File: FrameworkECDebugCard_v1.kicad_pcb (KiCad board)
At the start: 2 copper layers, 26 x 30 mm, 25 parts, among them J1 Conn_01x05, P1 USB_C_Plug_USB2.0, P2 USB_B_Micro, U1 FT230XS

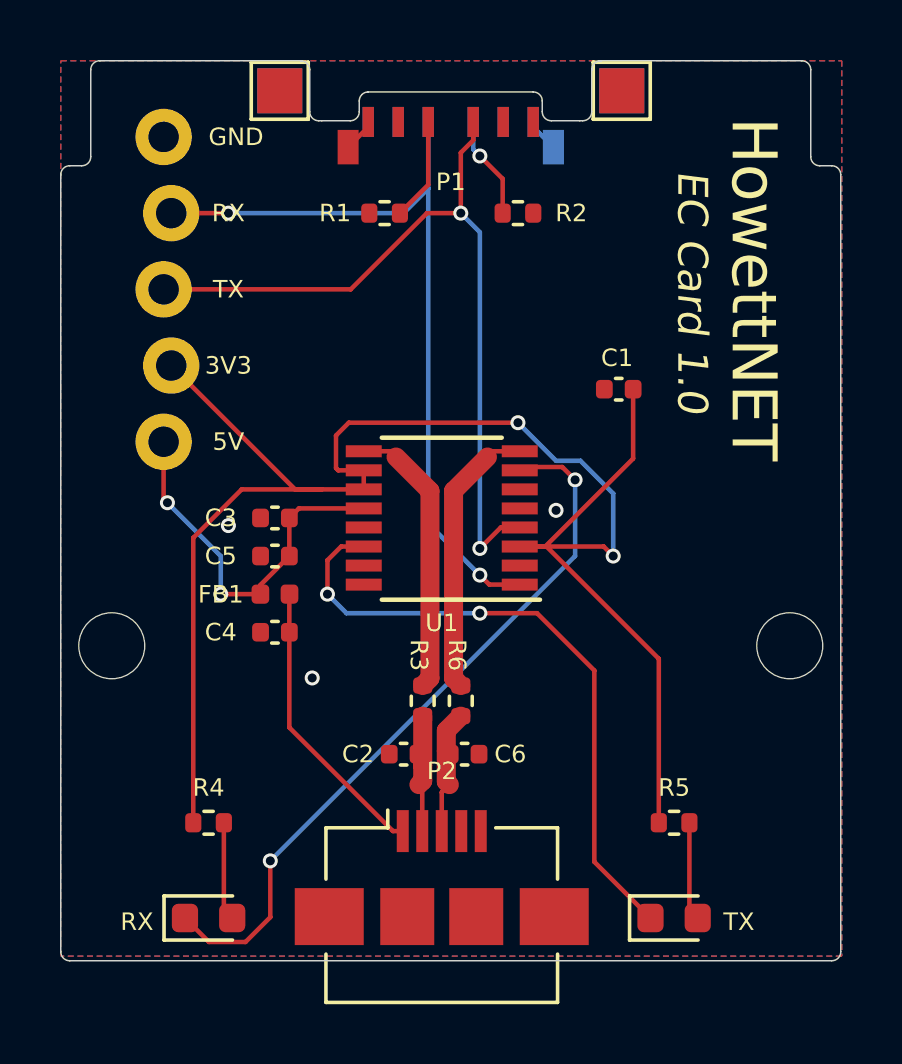
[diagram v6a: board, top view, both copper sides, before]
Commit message: Move the passives closer to USB, use 6mil traces to passives
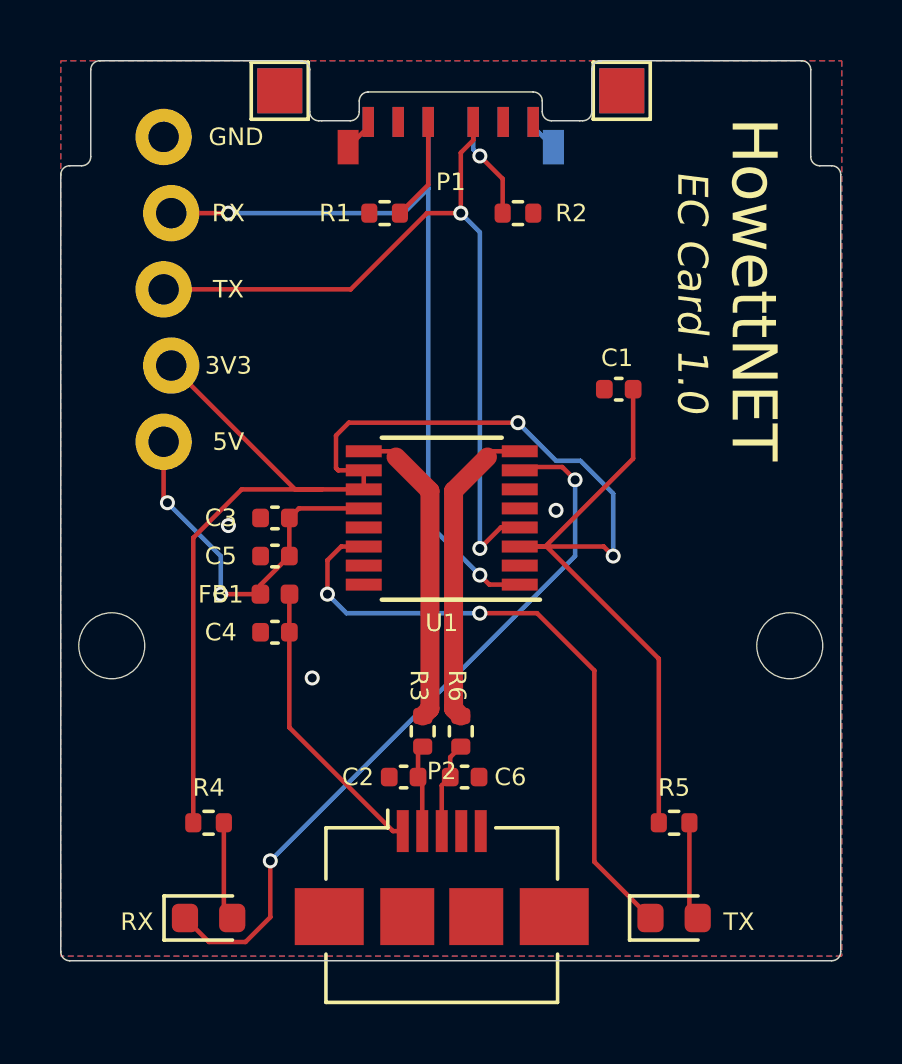
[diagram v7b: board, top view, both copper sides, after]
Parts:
- moved R3 1.02 mm to (139.1, 149.4)
- moved R6 1.02 mm to (140.3, 149.4)
- moved C2 0.76 mm to (138.4, 150.9)
- moved C6 0.76 mm to (140.5, 150.9)
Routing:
- net /USBD-: track 4.15 -> 2.94 mm
- net /USBD+: track 4.18 -> 3.08 mm
- net /F_USBD-: track 9.34 -> 10.4 mm
- net /F_USBD+: track 9.34 -> 10.4 mm
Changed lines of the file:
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@@
   )
   (footprint "Resistor_SMD:R_0402_1005Metric" (layer "F.Cu")
-    (at 139.065 148.336 90)
+    (at 139.065 149.352 90)
     (descr "Resistor SMD 0402 (1005 Metric), square (rectangular) end terminal, IPC_7351 nominal, (Body size source: IPC-SM-782 page 72, https://www.pcb-3d.com/wordpress/wp-content/uploads/ipc-sm-782a_amendment_1_and_2.pdf), generated with kicad-footprint-generator")
     (tags "resistor")
@@
   )
   (footprint "Resistor_SMD:R_0402_1005Metric" (layer "F.Cu")
-    (at 140.335 148.336 90)
+    (at 140.335 149.352 90)
     (descr "Resistor SMD 0402 (1005 Metric), square (rectangular) end terminal, IPC_7351 nominal, (Body size source: IPC-SM-782 page 72, https://www.pcb-3d.com/wordpress/wp-content/uploads/ipc-sm-782a_amendment_1_and_2.pdf), generated with kicad-footprint-generator")
     (tags "resistor")
@@
   )
   (footprint "Capacitor_SMD:C_0402_1005Metric" (layer "F.Cu")
-    (at 138.43 150.114 180)
+    (at 138.43 150.876 180)
     (descr "Capacitor SMD 0402 (1005 Metric), square (rectangular) end terminal, IPC_7351 nominal, (Body size source: IPC-SM-782 page 76, https://www.pcb-3d.com/wordpress/wp-content/uploads/ipc-sm-782a_amendment_1_and_2.pdf), generated with kicad-footprint-generator")
     (tags "capacitor")
@@
   )
   (footprint "Capacitor_SMD:C_0402_1005Metric" (layer "F.Cu")
-    (at 140.462 150.114)
+    (at 140.462 150.876)
     (descr "Capacitor SMD 0402 (1005 Metric), square (rectangular) end terminal, IPC_7351 nominal, (Body size source: IPC-SM-782 page 76, https://www.pcb-3d.com/wordpress/wp-content/uploads/ipc-sm-782a_amendment_1_and_2.pdf), generated with kicad-footprint-generator")
     (tags "capacitor")
@@
   (segment (start 132.334 143.51) (end 132.334 144.78) (width 0.1524) (layer "B.Cu") (net 8))
   (segment (start 130.556 141.732) (end 132.334 143.51) (width 0.1524) (layer "B.Cu") (net 8))
-  (segment (start 139.852001 149.328999) (end 139.852001 150.012001) (width 0.635) (layer "F.Cu") (net 9))
-  (segment (start 139.7 151.384) (end 139.954 151.13) (width 0.1524) (layer "F.Cu") (net 9))
-  (segment (start 140.335 148.846) (end 139.852001 149.328999) (width 0.635) (layer "F.Cu") (net 9))
-  (segment (start 139.852001 151.028001) (end 139.954 151.13) (width 0.635) (layer "F.Cu") (net 9))
-  (segment (start 139.7 152.6786) (end 139.7 151.384) (width 0.1524) (layer "F.Cu") (net 9))
-  (segment (start 139.852001 150.012001) (end 139.852001 151.028001) (width 0.635) (layer "F.Cu") (net 9))
-  (segment (start 139.05 152.6786) (end 139.05 151.242) (width 0.1524) (layer "F.Cu") (net 10))
-  (segment (start 139.065 151.003) (end 138.938 151.13) (width 0.635) (layer "F.Cu") (net 10))
-  (segment (start 138.91 150.34) (end 139.065 150.495) (width 0.1524) (layer "F.Cu") (net 10))
-  (segment (start 139.065 148.846) (end 139.065 150.495) (width 0.635) (layer "F.Cu") (net 10))
-  (segment (start 139.065 150.495) (end 139.065 151.003) (width 0.635) (layer "F.Cu") (net 10))
-  (segment (start 139.05 151.242) (end 138.938 151.13) (width 0.1524) (layer "F.Cu") (net 10))
+  (segment (start 139.982 150.215) (end 140.335 149.862) (width 0.1524) (layer "F.Cu") (net 9))
+  (segment (start 139.7 151.158) (end 139.7 152.6786) (width 0.1524) (layer "F.Cu") (net 9))
+  (segment (start 139.982 150.876) (end 139.982 150.215) (width 0.1524) (layer "F.Cu") (net 9))
+  (segment (start 139.982 150.876) (end 139.7 151.158) (width 0.1524) (layer "F.Cu") (net 9))
+  (segment (start 138.91 150.876) (end 138.91 150.017) (width 0.1524) (layer "F.Cu") (net 10))
+  (segment (start 138.91 150.876) (end 139.05 151.016) (width 0.1524) (layer "F.Cu") (net 10))
+  (segment (start 139.05 151.016) (end 139.05 152.6786) (width 0.1524) (layer "F.Cu") (net 10))
+  (segment (start 138.91 150.017) (end 139.065 149.862) (width 0.1524) (layer "F.Cu") (net 10))
   (segment (start 135.89 144.78) (end 135.89 143.6501) (width 0.1524) (layer "F.Cu") (net 11))
   (segment (start 135.89 143.6501) (end 136.3476 143.1925) (width 0.1524) (layer "F.Cu") (net 11))
@@
   (segment (start 144.145 143.51) (end 144.145 140.97) (width 0.1524) (layer "B.Cu") (net 12))
   (segment (start 133.985 153.67) (end 144.145 143.51) (width 0.1524) (layer "B.Cu") (net 12))
+  (segment (start 142.3 140.0175) (end 141.4145 140.0175) (width 0.1524) (layer "F.Cu") (net 13))
+  (segment (start 141.4145 140.0175) (end 141.224 140.208) (width 0.1524) (layer "F.Cu") (net 13))
   (segment (start 140.093501 141.338499) (end 141.224 140.208) (width 0.635) (layer "F.Cu") (net 13))
-  (segment (start 141.4145 140.0175) (end 141.224 140.208) (width 0.1524) (layer "F.Cu") (net 13))
-  (segment (start 140.093501 147.584501) (end 140.093501 141.338499) (width 0.635) (layer "F.Cu") (net 13))
-  (segment (start 140.335 147.826) (end 140.093501 147.584501) (width 0.635) (layer "F.Cu") (net 13))
-  (segment (start 142.3 140.0175) (end 141.4145 140.0175) (width 0.1524) (layer "F.Cu") (net 13))
+  (segment (start 140.335 148.842) (end 140.093501 148.600501) (width 0.635) (layer "F.Cu") (net 13))
+  (segment (start 140.093501 148.600501) (end 140.093501 141.338499) (width 0.635) (layer "F.Cu") (net 13))
+  (segment (start 139.306499 141.338499) (end 138.176 140.208) (width 0.635) (layer "F.Cu") (net 14))
+  (segment (start 139.306499 148.600501) (end 139.306499 141.338499) (width 0.635) (layer "F.Cu") (net 14))
+  (segment (start 139.065 148.842) (end 139.306499 148.600501) (width 0.635) (layer "F.Cu") (net 14))
+  (segment (start 137.9855 140.0175) (end 138.176 140.208) (width 0.1524) (layer "F.Cu") (net 14))
   (segment (start 137.1 140.0175) (end 137.9855 140.0175) (width 0.1524) (layer "F.Cu") (net 14))
-  (segment (start 139.065 147.826) (end 139.306499 147.584501) (width 0.635) (layer "F.Cu") (net 14))
-  (segment (start 139.306499 141.338499) (end 138.176 140.208) (width 0.635) (layer "F.Cu") (net 14))
-  (segment (start 137.9855 140.0175) (end 138.176 140.208) (width 0.1524) (layer "F.Cu") (net 14))
-  (segment (start 139.306499 147.584501) (end 139.306499 141.338499) (width 0.635) (layer "F.Cu") (net 14))
   (segment (start 143.1925 143.1925) (end 142.3 143.1925) (width 0.1524) (layer "F.Cu") (net 15))
   (segment (start 142.3 143.1925) (end 145.0975 143.1925) (width 0.1524) (layer "F.Cu") (net 15))

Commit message: Re-route VCCIO to move cap closer to 3V3OUT, reroute RXLED in the new space
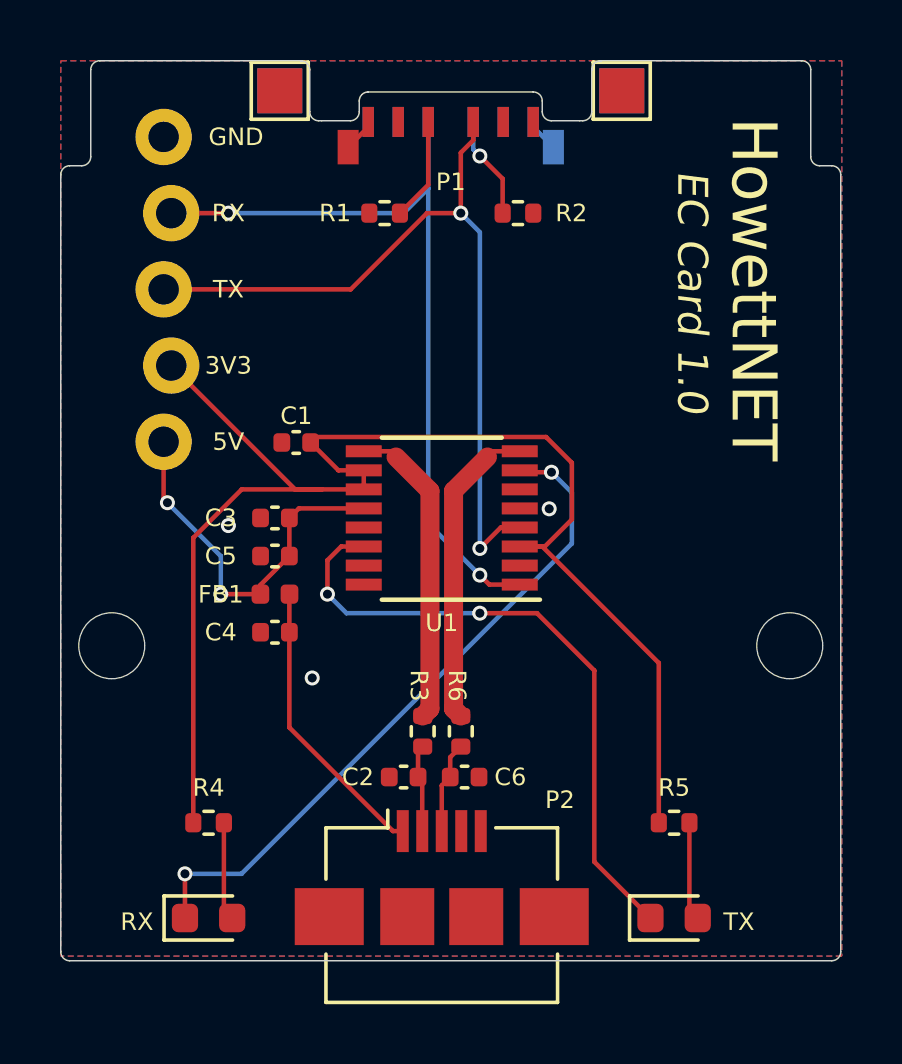
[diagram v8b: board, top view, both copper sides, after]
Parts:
- moved C1 10.9 mm to (134.8, 139.7)
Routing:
- net VCCIO: track 59.9 -> 50.1 mm, vias 2 -> 0
- net /RXLED: track 23.8 -> 22.7 mm
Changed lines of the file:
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@@
     (property "Sheetname" "")
     (attr smd)
-    (fp_text reference "P2" (at 0 -3.55 unlocked) (layer "F.SilkS")
+    (fp_text reference "P2" (at 3.937 -2.5906 unlocked) (layer "F.SilkS")
       (effects (font (size 0.5842 0.5842) (thickness 0.1016)))
     )
@@
   )
   (footprint "Capacitor_SMD:C_0402_1005Metric" (layer "F.Cu")
-    (at 145.6 137.9482 180)
+    (at 134.8486 139.7254 180)
     (descr "Capacitor SMD 0402 (1005 Metric), square (rectangular) end terminal, IPC_7351 nominal, (Body size source: IPC-SM-782 page 76, https://www.pcb-3d.com/wordpress/wp-content/uploads/ipc-sm-782a_amendment_1_and_2.pdf), generated with kicad-footprint-generator")
     (tags "capacitor")
@@
     (property "Sheetname" "")
     (attr smd)
-    (fp_text reference "C1" (at 0.058 1.0422 180) (layer "F.SilkS")
+    (fp_text reference "C1" (at -0.0026 0.889) (layer "F.SilkS")
       (effects (font (size 0.5842 0.5842) (thickness 0.1016)))
     )
@@
   (segment (start 137.25 129.04) (end 137.25 129.21) (width 0.1524) (layer "F.Cu") (net 1))
   (via (at 132.588 142.494) (size 0.5) (drill 0.3) (layers "F.Cu" "B.Cu") (free) (net 1))
-  (via (at 143.51 141.986) (size 0.5) (drill 0.3) (layers "F.Cu" "B.Cu") (free) (net 1))
+  (via (at 143.2814 141.9352) (size 0.5) (drill 0.3) (layers "F.Cu" "B.Cu") (free) (net 1))
   (via (at 135.382 147.574) (size 0.5) (drill 0.3) (layers "F.Cu" "B.Cu") (free) (net 1))
   (segment (start 142.75 129.21) (end 143.42 129.88) (width 0.1524) (layer "B.Cu") (net 1))
@@
   (segment (start 136.525 145.415) (end 135.89 144.78) (width 0.1524) (layer "B.Cu") (net 11))
   (segment (start 140.97 145.415) (end 136.525 145.415) (width 0.1524) (layer "B.Cu") (net 11))
-  (segment (start 133.985 155.548979) (end 133.985 153.67) (width 0.1524) (layer "F.Cu") (net 12))
-  (segment (start 143.7175 140.5425) (end 142.875 140.5425) (width 0.1524) (layer "F.Cu") (net 12))
-  (segment (start 133.158979 156.375) (end 133.985 155.548979) (width 0.1524) (layer "F.Cu") (net 12))
-  (segment (start 131.14 155.575) (end 131.94 156.375) (width 0.1524) (layer "F.Cu") (net 12))
-  (segment (start 144.145 140.97) (end 143.7175 140.5425) (width 0.1524) (layer "F.Cu") (net 12))
-  (segment (start 131.94 156.375) (end 133.158979 156.375) (width 0.1524) (layer "F.Cu") (net 12))
-  (via (at 144.145 140.97) (size 0.5) (drill 0.3) (layers "F.Cu" "B.Cu") (net 12))
-  (via (at 133.985 153.67) (size 0.5) (drill 0.3) (layers "F.Cu" "B.Cu") (net 12))
-  (segment (start 144.145 143.51) (end 144.145 140.97) (width 0.1524) (layer "B.Cu") (net 12))
-  (segment (start 133.985 153.67) (end 144.145 143.51) (width 0.1524) (layer "B.Cu") (net 12))
+  (segment (start 142.3635 140.716) (end 142.3 140.6525) (width 0.1524) (layer "F.Cu") (net 12))
+  (segment (start 131.14 154.102) (end 131.1402 154.1018) (width 0.1524) (layer "F.Cu") (net 12))
+  (segment (start 143.3576 140.716) (end 142.3635 140.716) (width 0.1524) (layer "F.Cu") (net 12))
+  (segment (start 131.14 155.575) (end 131.14 154.102) (width 0.1524) (layer "F.Cu") (net 12))
+  (via (at 131.1402 154.1018) (size 0.5) (drill 0.3) (layers "F.Cu" "B.Cu") (net 12))
+  (via (at 143.3576 140.716) (size 0.5) (drill 0.3) (layers "F.Cu" "B.Cu") (net 12))
+  (segment (start 133.02736 154.1018) (end 144.0362 143.09296) (width 0.1524) (layer "B.Cu") (net 12))
+  (segment (start 131.1402 154.1018) (end 133.02736 154.1018) (width 0.1524) (layer "B.Cu") (net 12))
+  (segment (start 144.0362 143.09296) (end 144.0362 141.3946) (width 0.1524) (layer "B.Cu") (net 12))
+  (segment (start 144.0362 141.3946) (end 143.3576 140.716) (width 0.1524) (layer "B.Cu") (net 12))
   (segment (start 142.3 140.0175) (end 141.4145 140.0175) (width 0.1524) (layer "F.Cu") (net 13))
   (segment (start 141.4145 140.0175) (end 141.224 140.208) (width 0.1524) (layer "F.Cu") (net 13))
@@
   (segment (start 137.9855 140.0175) (end 138.176 140.208) (width 0.1524) (layer "F.Cu") (net 14))
   (segment (start 137.1 140.0175) (end 137.9855 140.0175) (width 0.1524) (layer "F.Cu") (net 14))
-  (segment (start 143.1925 143.1925) (end 142.3 143.1925) (width 0.1524) (layer "F.Cu") (net 15))
-  (segment (start 142.3 143.1925) (end 145.0975 143.1925) (width 0.1524) (layer "F.Cu") (net 15))
-  (segment (start 146.935 146.935) (end 143.1925 143.1925) (width 0.1524) (layer "F.Cu") (net 15))
-  (segment (start 136.175 139.4925) (end 136.175 140.5775) (width 0.1524) (layer "F.Cu") (net 15))
+  (segment (start 137.1 140.6525) (end 136.2557 140.6525) (width 0.1524) (layer "F.Cu") (net 15))
   (segment (start 130.683 137.16) (end 134.8105 141.2875) (width 0.1524) (layer "F.Cu") (net 15))
-  (segment (start 143.15 143.1925) (end 146.08 140.2625) (width 0.1524) (layer "F.Cu") (net 15))
-  (segment (start 146.08 140.2625) (end 146.08 137.9482) (width 0.1524) (layer "F.Cu") (net 15))
+  (segment (start 143.0524 143.1925) (end 146.935 147.0751) (width 0.1524) (layer "F.Cu") (net 15))
+  (segment (start 144.0362 140.4013) (end 144.0362 142.2917) (width 0.1524) (layer "F.Cu") (net 15))
+  (segment (start 135.3286 139.7254) (end 135.5127 139.5413) (width 0.1524) (layer "F.Cu") (net 15))
   (segment (start 131.4175 142.9025) (end 131.4175 152.4) (width 0.1524) (layer "F.Cu") (net 15))
   (segment (start 137.1 141.2875) (end 137.1 140.6525) (width 0.1524) (layer "F.Cu") (net 15))
-  (segment (start 136.25 140.6525) (end 137.1 140.6525) (width 0.1524) (layer "F.Cu") (net 15))
+  (segment (start 143.1354 143.1925) (end 142.3 143.1925) (width 0.1524) (layer "F.Cu") (net 15))
+  (segment (start 144.0362 142.2917) (end 143.1354 143.1925) (width 0.1524) (layer "F.Cu") (net 15))
   (segment (start 135.6995 141.2875) (end 133.0325 141.2875) (width 0.1524) (layer "F.Cu") (net 15))
   (segment (start 133.0325 141.2875) (end 131.4175 142.9025) (width 0.1524) (layer "F.Cu") (net 15))
   (segment (start 134.8105 141.2875) (end 135.6995 141.2875) (width 0.1524) (layer "F.Cu") (net 15))
-  (segment (start 142.3 143.1925) (end 143.15 143.1925) (width 0.1524) (layer "F.Cu") (net 15))
-  (segment (start 145.0975 143.1925) (end 145.415 143.51) (width 0.1524) (layer "F.Cu") (net 15))
+  (segment (start 142.3 143.1925) (end 143.0524 143.1925) (width 0.1524) (layer "F.Cu") (net 15))
   (segment (start 137.1 141.2875) (end 135.6995 141.2875) (width 0.1524) (layer "F.Cu") (net 15))
-  (segment (start 136.175 140.5775) (end 136.25 140.6525) (width 0.1524) (layer "F.Cu") (net 15))
-  (segment (start 142.24 139.065) (end 136.6025 139.065) (width 0.1524) (layer "F.Cu") (net 15))
-  (segment (start 136.6025 139.065) (end 136.175 139.4925) (width 0.1524) (layer "F.Cu") (net 15))
-  (segment (start 146.935 152.4) (end 146.935 146.935) (width 0.1524) (layer "F.Cu") (net 15))
-  (via (at 142.24 139.065) (size 0.5) (drill 0.3) (layers "F.Cu" "B.Cu") (net 15))
-  (via (at 145.415 143.51) (size 0.5) (drill 0.3) (layers "F.Cu" "B.Cu") (net 15))
-  (segment (start 143.51 140.335) (end 142.24 139.065) (width 0.1524) (layer "B.Cu") (net 15))
-  (segment (start 145.415 143.51) (end 145.415 141.426827) (width 0.1524) (layer "B.Cu") (net 15))
-  (segment (start 145.415 141.426827) (end 144.323173 140.335) (width 0.1524) (layer "B.Cu") (net 15))
-  (segment (start 144.323173 140.335) (end 143.51 140.335) (width 0.1524) (layer "B.Cu") (net 15))
+  (segment (start 143.1762 139.5413) (end 144.0362 140.4013) (width 0.1524) (layer "F.Cu") (net 15))
+  (segment (start 135.5127 139.5413) (end 143.1762 139.5413) (width 0.1524) (layer "F.Cu") (net 15))
+  (segment (start 146.935 147.0751) (end 146.935 152.4) (width 0.1524) (layer "F.Cu") (net 15))
+  (segment (start 136.2557 140.6525) (end 135.3286 139.7254) (width 0.1524) (layer "F.Cu") (net 15))
   (segment (start 130.429 134.62) (end 136.666525 134.62) (width 0.1524) (layer "F.Cu") (net 16))
   (segment (start 140.335 132.08) (end 140.335 130.06584) (width 0.1524) (layer "F.Cu") (net 16))
